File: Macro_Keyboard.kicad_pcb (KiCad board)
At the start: 6 copper layers, 109.7 x 84.3 mm, 103 parts, among them J1 USB_C_Receptacle_USB2.0, J2 USB_A, J3 USB_A, J4 USB_A, SW1 SW_Push, SW10 SW_DIP_x01, SW2 SW_DIP_x01, SW3 SW_DIP_x01, SW4 SW_DIP_x01, SW5 SW_DIP_x01, SW6 SW_DIP_x01, SW7 SW_DIP_x01, SW8 SW_DIP_x01, SW9 SW_DIP_x01, U1 STM32L432KCUx, U2 LD39050PU33R, U5 SRV05-4, U6 SRV05-4, Y1 12MHz

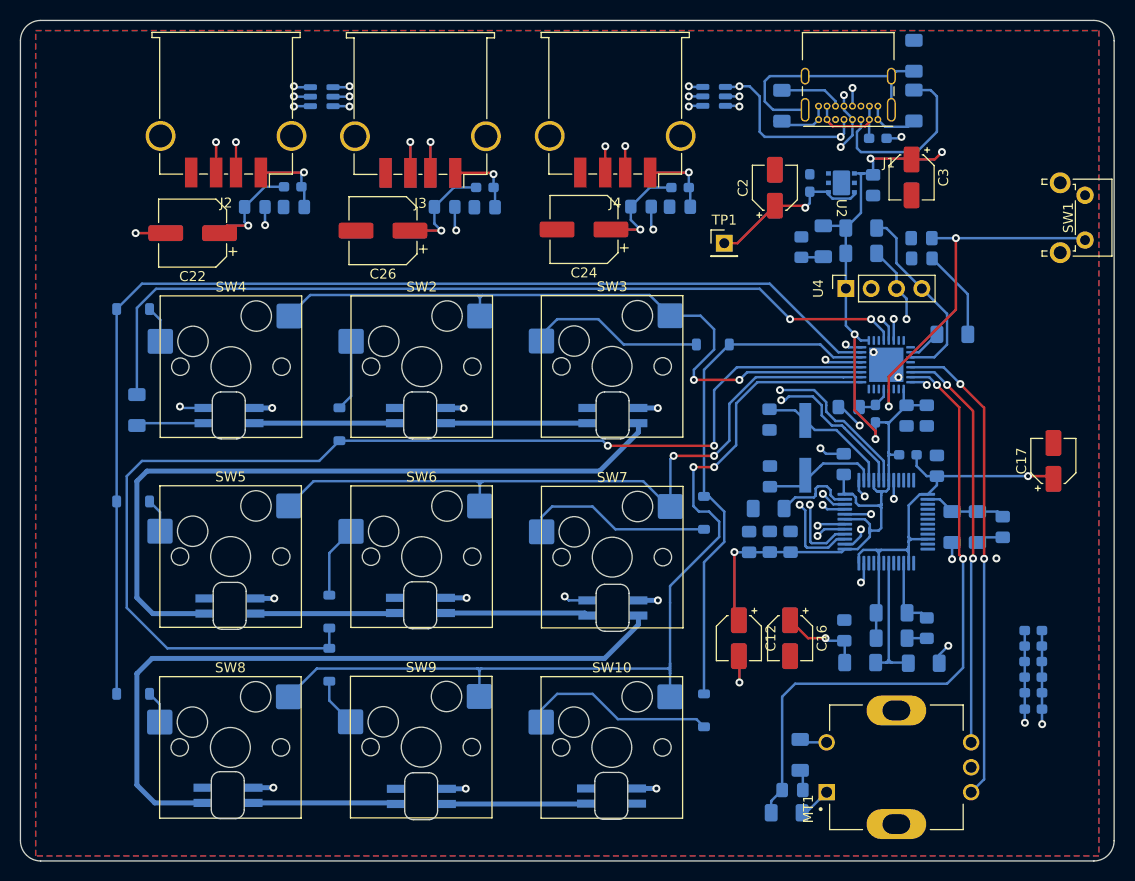
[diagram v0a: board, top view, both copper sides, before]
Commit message: Neue Anordnung für bessere Usb Leitungen
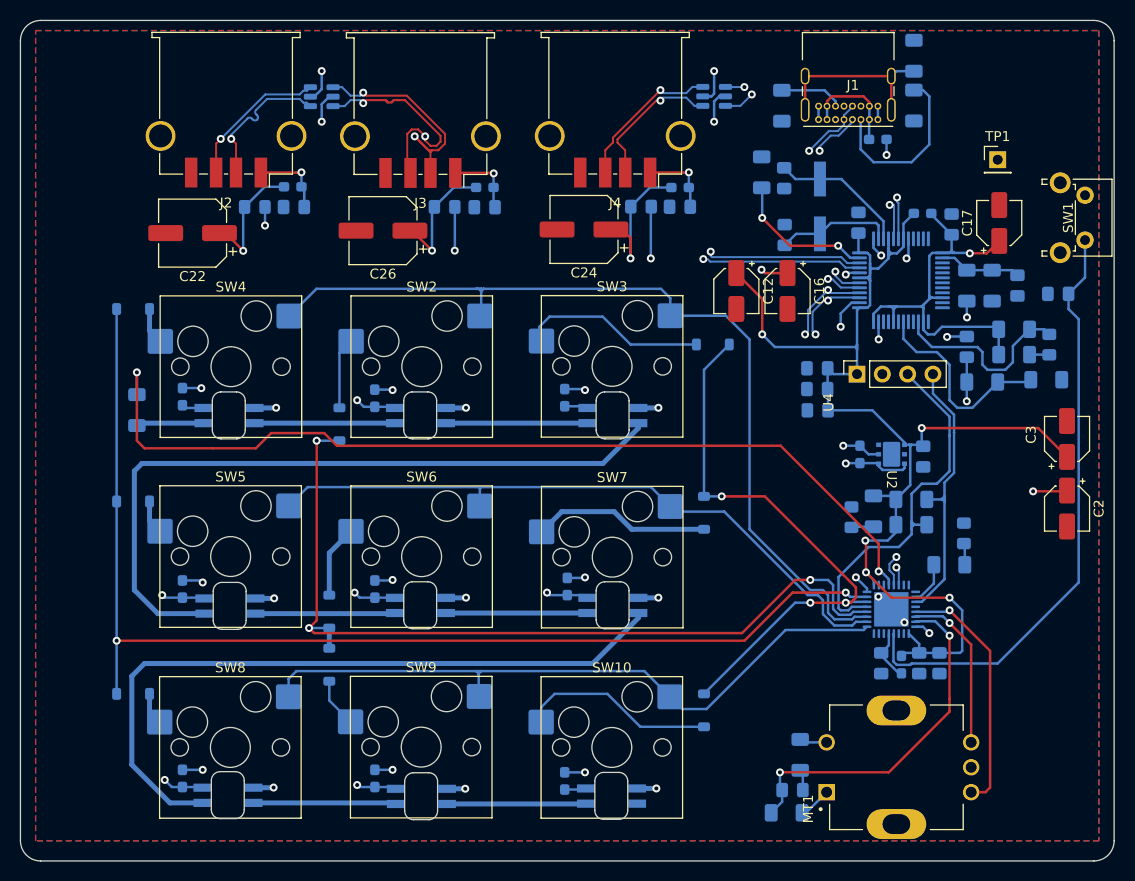
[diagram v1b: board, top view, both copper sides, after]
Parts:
- added C34: tbd, Capacitor_SMD:C_0603_1608Metric_Pad1.08x0.95mm_HandSolder, B.Cu at (73.2, 115.7)
- added C35: tbd, Capacitor_SMD:C_0603_1608Metric_Pad1.08x0.95mm_HandSolder, B.Cu at (92.5, 115.7)
- added C36: tbd, Capacitor_SMD:C_0603_1608Metric_Pad1.08x0.95mm_HandSolder, B.Cu at (111.5, 115.9)
- moved C33 88.5 mm to (73.2, 77.4), turned to -90 degrees
- moved C30 85.8 mm to (73.2, 96.7), turned to -90 degrees
- moved C32 70.6 mm to (92.4, 77.5), turned to -90 degrees
- moved C28 66.9 mm to (92.5, 96.7), turned to -90 degrees
- moved C31 53.9 mm to (111.5, 77.5), turned to -90 degrees
- moved C25 48.4 mm to (111.8, 96.4), turned to -90 degrees
- moved C2 43.5 mm to (161.9, 88.6), turned to -90 degrees
- moved C12 34.8 mm to (128.7, 66.8)
- moved C16 34.8 mm to (133.9, 66.8)
- moved R5 33.7 mm to (131.3, 54.9), turned to -90 degrees
- moved D3 31.0 mm to (160.1, 72.1)
- moved R8 31.0 mm to (156.6, 70.6)
- moved C15 31.0 mm to (151.8, 72.4)
- moved R11 31.0 mm to (159.8, 75.7)
- moved R9 31.0 mm to (156.6, 73.2)
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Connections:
- net /USB/DM1 renamed /USB/D_N1
- net /USB/DM2 renamed /USB/D_N2
- net /USB/DM3 renamed /USB/D_N3
- net /USB/DP1 renamed /USB/D_P1
- net /USB/DP2 renamed /USB/D_P2
- net /USB/DP3 renamed /USB/D_P3
- net USBDM renamed USBD_N
- net USBDP renamed USBD_P
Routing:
- net COL 1: track 119.2 -> 86.9 mm, vias 2 -> 3
- net Net-(U1-PH3): track 63.9 -> 35.8 mm
- net +3.3V: track 102.8 -> 128.6 mm
- net ROW 2: track 93.4 -> 68.5 mm, vias 2 -> 0
- net Rotary_B: track 41.2 -> 16.6 mm, vias 2 -> 1
- net Net-(U1-NRST): track 36.9 -> 60.4 mm, vias 2 -> 0
- net Rotary_A: track 48.2 -> 25.0 mm, vias 2 -> 1
- net ROW 0: track 70.6 -> 89.9 mm, vias 2 -> 0
- net SCK: track 22.9 -> 38.1 mm, vias 2 -> 0
- net /USB/D_P3: track 62.5 -> 47.6 mm, vias 3 -> 2
- net /USB/D_N3: track 59.7 -> 46.7 mm, vias 3 -> 2
- net /USB/PGANG: track 7.31 -> 19.4 mm
- net +5V: track 66.8 -> 76.0 mm, vias 20 -> 30
- net SDA: track 19.4 -> 28.2 mm
- net USBD_N: track 89.8 -> 81.6 mm
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
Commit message: Add files via upload
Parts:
- C10, C11, C13, C14, C15, C18, C19, C20, C21, C23, C27, C29, C9, D3, FB2, FB3, FB4, FB5, FB6, R10, R11, R12, R13, R17, R2, R3, R5, R6, R7, R8, R9, TH1, TH2, TH4, U3, U5, U6, Y1: moved to F.Cu
- C2, C3: moved to B.Cu
- moved C3 91.4 mm to (72.9, 60.6)
- moved C2 77.6 mm to (89.2, 61.2)
- moved C4 73.3 mm to (77.4, 61.8), turned to 90 degrees
- moved TP1 72.0 mm to (128.0, 120.3)
- moved U2 67.1 mm to (80.6, 62.1), turned to -90 degrees
- moved C1 61.1 mm to (83.7, 62.1), turned to -90 degrees
- moved TH1 44.2 mm to (124.5, 61.2)
- moved TH4 40.8 mm to (78.7, 63.8), turned to -90 degrees
- moved J2 39.4 mm to (116.9, 48.5)
- moved C22 39.4 mm to (113.6, 61.0)
- moved C23 39.4 mm to (123.7, 56.6), turned to 0 degrees
- moved C24 39.4 mm to (74.1, 60.6)
- moved J4 39.4 mm to (77.2, 48.5)
- moved U6 39.3 mm to (87.2, 47.0)
- moved C29 39.0 mm to (84.1, 56.9), turned to 0 degrees
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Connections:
- U5 pad 1: /USB/D_N2 -> /USB/D_P2
- U5 pad 3: /USB/D_P2 -> /USB/D_N2
- U5 pad 4: /USB/D_N1 -> /USB/D_P1
- U5 pad 6: /USB/D_P1 -> /USB/D_N1
- U6 pad 1: USBD_N -> USBD_P
- U6 pad 3: USBD_P -> USBD_N
- U6 pad 4: /USB/D_N3 -> /USB/D_P3
- U6 pad 6: /USB/D_P3 -> /USB/D_N3
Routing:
- net /USB/D_P1: track 96.7 -> 34.2 mm, vias 2 -> 0
- net /USB/D_N1: track 96.6 -> 34.2 mm, vias 2 -> 0
- net Net-(U1-NRST): track 60.4 -> 3.04 mm
- net GND: track 62.0 -> 9.63 mm, vias 18 -> 3
- net +3.3V: track 128.6 -> 84.1 mm, vias 5 -> 0
- net /USB/D_N3: track 46.7 -> 86.0 mm, vias 2 -> 0
- net /USB/D_P3: track 47.6 -> 86.2 mm, vias 2 -> 0
- net Net-(U1-PH3): track 35.8 -> 0.00 mm, vias 2 -> 0
- net ROW 0: track 89.9 -> 57.7 mm, vias 0 -> 2
- net Rotary_A: track 25.0 -> 0.00 mm, vias 1 -> 0
- net /USB/D_N2: track 77.7 -> 56.9 mm, vias 3 -> 0
- net /USB/D_P2: track 77.1 -> 57.0 mm, vias 3 -> 0
- net /USB/X1: track 11.8 -> 30.6 mm, vias 0 -> 2
- net ROW 2: track 68.5 -> 85.7 mm, vias 0 -> 2
- net Rotary_B: track 16.6 -> 0.00 mm, vias 1 -> 0
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- removed copper zone on In4.Cu, net GND
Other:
- board size 109.7 x 84.3 mm -> 95.6 x 84.2 mm
- copper layers 6 -> 4

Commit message: Add files via upload
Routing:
- net +3.3V: track 84.1 -> 174.9 mm, vias 0 -> 4
- net Net-(U1-NRST): track 3.04 -> 74.5 mm, vias 0 -> 2
- net GND: track 9.63 -> 75.5 mm, vias 3 -> 20
- net Net-(U1-PH3): track 0.00 -> 65.5 mm, vias 0 -> 1
- net Rotary_A: track 0.00 -> 62.0 mm, vias 0 -> 1
- net Rotary_B: track 0.00 -> 54.7 mm, vias 0 -> 1
- net Net-(J2-VBUS): track 0.00 -> 19.8 mm, vias 0 -> 2
- net Net-(U3-RREF): track 0.00 -> 14.2 mm, vias 0 -> 2
- net Net-(C22-Pad1): track 0.00 -> 8.57 mm
- net BOOT: track 0.00 -> 7.74 mm
- net +5V: track 70.1 -> 75.9 mm, vias 24 -> 27
- net Net-(FB6-Pad1): track 4.91 -> 10.3 mm
- net Net-(MT1-Pad2): track 0.00 -> 4.10 mm
- net USBD_N: track 86.6 -> 88.9 mm
- net USBD_P: track 86.6 -> 88.9 mm
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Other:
- board text added: "TODO if Route is okay: .) Name .) Silkscreen .) DRC"

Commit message: Add files via upload
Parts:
- removed C10, C11, C13, C18: 0.1uF, Capacitor_SMD:C_0805_2012Metric_Pad1.18x1.45mm_HandSolder
- removed C12: 1uF, Capacitor_SMD:CP_Elec_4x5.4
- removed C17: 10uF, Capacitor_SMD:CP_Elec_4x5.8
- removed FB5: BLM18BA, Inductor_SMD:L_0603_1608Metric_Pad1.05x0.95mm_HandSolder
- added C37: 1uF, Capacitor_SMD:C_0603_1608Metric_Pad1.08x0.95mm_HandSolder, F.Cu at (134.5, 54.4)
- added C38: 1uF, Capacitor_SMD:C_0603_1608Metric_Pad1.08x0.95mm_HandSolder, F.Cu at (134.6, 56.1)
- added C39: 1uF, Capacitor_SMD:C_0603_1608Metric_Pad1.08x0.95mm_HandSolder, F.Cu at (130.8, 56.1)
- added C40: 1uF, Capacitor_SMD:C_0603_1608Metric_Pad1.08x0.95mm_HandSolder, F.Cu at (134.5, 50.9)
- added C41: 0.1uF, Capacitor_SMD:C_0603_1608Metric_Pad1.08x0.95mm_HandSolder, F.Cu at (134.5, 49.2)
- added C42: 0.1uF, Capacitor_SMD:C_0603_1608Metric_Pad1.08x0.95mm_HandSolder, F.Cu at (130.8, 52.6)
- added FB7: BLM18BA, Inductor_SMD:L_0603_1608Metric_Pad1.05x0.95mm_HandSolder, F.Cu at (134.5, 52.6)
- added FB8: BLM18BA, Inductor_SMD:L_0603_1608Metric_Pad1.05x0.95mm_HandSolder, F.Cu at (130.8, 54.4)
- C14: value 0.1uF -> 10uF; footprint Capacitor_SMD:C_0805_2012Metric_Pad1.18x1.45mm_HandSolder -> Capacitor_SMD:CP_Elec_4x5.8; moved to B.Cu
- C15, C19, C23, C27, C29, C4, C5, C6, C7, C8, C9: footprint Capacitor_SMD:C_0805_2012Metric_Pad1.18x1.45mm_HandSolder -> Capacitor_SMD:C_0603_1608Metric_Pad1.08x0.95mm_HandSolder
- C16, C2, C3: footprint Capacitor_SMD:CP_Elec_4x5.4 -> Capacitor_SMD:C_0603_1608Metric_Pad1.08x0.95mm_HandSolder
- C20, C21: footprint Capacitor_SMD:C_0805_2012Metric_Pad1.18x1.45mm_HandSolder -> Capacitor_SMD:C_0603_1608Metric_Pad1.08x0.95mm_HandSolder; moved to B.Cu
- R1, R10, R11, R12, R13, R15, R16, R17, R2, R3, R4, R5, R6, R7, R8, R9: footprint Resistor_SMD:R_1206_3216Metric_Pad1.30x1.75mm_HandSolder -> Resistor_SMD:R_0805_2012Metric_Pad1.20x1.40mm_HandSolder
- Y1: moved to B.Cu
- moved C3 80.9 mm to (151.0, 81.8), turned to 180 degrees
- moved C4 75.9 mm to (151.1, 79.7), turned to 180 degrees
- moved U2 72.0 mm to (151.1, 76.2), turned to 0 degrees
- moved C1 68.4 mm to (151.3, 72.9), turned to 0 degrees
- moved C2 62.8 mm to (151.3, 70.9), turned to 0 degrees
- moved U4 29.7 mm to (145.8, 104.4), turned to -90 degrees
- moved C14 23.4 mm to (151.6, 85.3), turned to 180 degrees
- moved C21 22.0 mm to (142.0, 71.9), turned to 0 degrees
- moved C20 20.5 mm to (135.7, 72.0), turned to 180 degrees
- moved Y1 19.2 mm to (138.9, 68.6), turned to 0 degrees
- moved C16 19.2 mm to (138.5, 53.6), turned to 90 degrees
- moved R4 15.4 mm to (144.8, 78.0), turned to 0 degrees
- moved C6 15.0 mm to (137.4, 90.8), turned to 180 degrees
- moved C7 13.8 mm to (137.4, 89.0), turned to 180 degrees
- moved D2 13.2 mm to (144.8, 75.8), turned to 0 degrees
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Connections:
- C14 pad 1: DVDD -> +3.3V
- U3 pad 1: +3.3V -> AVDD
- U3 pad 12: +3.3V -> AVDD
- U3 pad 16: +3.3V -> AVDD
- U3 pad 19: +3.3V -> AVDD
- U3 pad 7: +3.3V -> AVDD
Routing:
- net +3.3V: track 174.9 -> 0.00 mm, vias 4 -> 0
- net COL 0: track 106.9 -> 0.00 mm
- net USBD_N: track 88.9 -> 0.00 mm, vias 1 -> 0
- net USBD_P: track 88.9 -> 0.00 mm, vias 1 -> 0
- net /USB/D_P3: track 86.2 -> 0.00 mm
- net /USB/D_N3: track 86.0 -> 0.00 mm
- net ROW 2: track 85.7 -> 0.00 mm, vias 2 -> 0
- net COL 1: track 81.9 -> 0.00 mm, vias 3 -> 0
- net LED: track 80.2 -> 0.00 mm, vias 2 -> 0
- net +5V: track 75.9 -> 0.00 mm, vias 27 -> 0
- net GND: track 75.5 -> 0.00 mm, vias 20 -> 0
- net Net-(U1-NRST): track 74.5 -> 0.00 mm, vias 2 -> 0
- net Net-(SK6812MINI_E3-DOUT): track 73.0 -> 0.00 mm
- net Net-(SK6812MINI_E6-DOUT): track 71.7 -> 0.00 mm
- net ROW 1: track 68.3 -> 0.00 mm, vias 2 -> 0
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- removed copper zone on In2.Cu, net +5V
- removed copper zone on B.Cu, net GND
- removed copper zone on F.Cu, net GND
- removed copper zone on In1.Cu, net GND
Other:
- board text removed: "TODO if Route is okay: .) Name .) Silkscreen .) DRC"

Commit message: Add files via upload
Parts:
- added C10: 0.1uF, Capacitor_SMD:C_0603_1608Metric_Pad1.08x0.95mm_HandSolder, B.Cu at (135.7, 49.3)
- added C11: 0.1uF, Capacitor_SMD:C_0603_1608Metric_Pad1.08x0.95mm_HandSolder, B.Cu at (135.7, 51.0)
- added C12: 0.1uF, Capacitor_SMD:C_0603_1608Metric_Pad1.08x0.95mm_HandSolder, B.Cu at (135.7, 52.7)
- added C13: 0.1uF, Capacitor_SMD:C_0603_1608Metric_Pad1.08x0.95mm_HandSolder, B.Cu at (135.7, 54.5)
- added C17: 0.1uF, Capacitor_SMD:C_0603_1608Metric_Pad1.08x0.95mm_HandSolder, F.Cu at (135.7, 49.3)
- added C18: 0.1uF, Capacitor_SMD:C_0603_1608Metric_Pad1.08x0.95mm_HandSolder, F.Cu at (135.7, 51.0)
- added C43: 0.1uF, Capacitor_SMD:C_0603_1608Metric_Pad1.08x0.95mm_HandSolder, F.Cu at (135.7, 52.7)
- added C44: 0.1uF, Capacitor_SMD:C_0603_1608Metric_Pad1.08x0.95mm_HandSolder, F.Cu at (135.7, 54.5)
- C22, C23, C38, C39, C42, FB3, FB8, TH1: moved to B.Cu
- moved C29 18.5 mm to (66.5, 54.5), turned to 90 degrees
- moved FB4 14.7 mm to (66.4, 57.9), turned to -90 degrees
- moved TH4 13.0 mm to (68.3, 57.7), turned to 90 degrees
- moved C23 12.4 mm to (112.4, 61.3), turned to 180 degrees
- moved TH1 9.19 mm to (112.3, 57.9)
- moved FB3 8.83 mm to (112.4, 59.7)
- moved C22 8.49 mm to (105.7, 57.9)
- moved FB2 7.84 mm to (93.1, 61.2)
- moved C27 7.80 mm to (96.5, 61.2)
- moved TH2 5.95 mm to (94.5, 59.2)
- moved C26 5.84 mm to (87.6, 59.2)
- moved C39 3.72 mm to (132.3, 52.7)
- moved FB8 3.67 mm to (132.3, 51.0), turned to 0 degrees
- moved C42 3.59 mm to (132.2, 49.3), turned to 0 degrees
- moved C38 2.79 mm to (132.3, 54.5)
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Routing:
- net +3.3V: track 0.00 -> 119.0 mm, vias 0 -> 4
- net COL 0: track 0.00 -> 109.7 mm, vias 0 -> 2
- net +5V: track 0.00 -> 97.1 mm, vias 0 -> 25
- net USBD_P: track 0.00 -> 92.7 mm, vias 0 -> 1
- net USBD_N: track 0.00 -> 92.0 mm, vias 0 -> 1
- net LED: track 0.00 -> 89.2 mm, vias 0 -> 2
- net /USB/D_N3: track 0.00 -> 88.4 mm
- net /USB/D_P3: track 0.00 -> 87.2 mm
- net ROW 2: track 0.00 -> 81.8 mm, vias 0 -> 2
- net GND: track 0.00 -> 78.8 mm, vias 0 -> 26
- net Net-(SK6812MINI_E3-DOUT): track 0.00 -> 73.7 mm
- net Net-(SK6812MINI_E6-DOUT): track 0.00 -> 71.6 mm
- net COL 1: track 0.00 -> 70.7 mm, vias 0 -> 2
- net ROW 0: track 0.00 -> 70.2 mm, vias 0 -> 4
- net ROW 1: track 0.00 -> 67.3 mm, vias 0 -> 2
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- added copper zone on In2.Cu, net +5V
- added copper zone on B.Cu, net AVDD
- added copper zone on In2.Cu, net DVDD
- added copper zone on B.Cu, net GND
- added copper zone on F.Cu, net GND
- added copper zone on In1.Cu, net GND

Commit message: Add files via upload
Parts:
- C22, C23, FB3, TH1: moved to F.Cu
- moved SK6812MINI_E7 42.2 mm to (118.1, 118.8), turned to 180 degrees
- moved SK6812MINI_E1 42.1 mm to (118.2, 80.7), turned to 180 degrees
- moved SK6812MINI_E4 42.0 mm to (118.1, 99.8), turned to 180 degrees
- moved SK6812MINI_E3 35.1 mm to (79.7, 80.7), turned to 180 degrees
- moved SK6812MINI_E6 35.1 mm to (79.7, 99.8), turned to 180 degrees
- moved SK6812MINI_E9 35.0 mm to (79.7, 118.8), turned to 180 degrees
- moved U5 25.6 mm to (130.3, 57.4), turned to 180 degrees
- moved R15 13.7 mm to (137.4, 92.7), turned to 180 degrees
- moved D8 6.77 mm to (87.1, 105.7)
- moved D9 6.77 mm to (87.1, 111.0)
- moved R5 6.44 mm to (128.3, 68.6), turned to 90 degrees
- moved C28 6.06 mm to (87.4, 93.4)
- moved D3 4.80 mm to (153.9, 62.0)
- moved R8 4.80 mm to (152.9, 58.9)
- moved R9 4.80 mm to (155.0, 58.9)
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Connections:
- J1 pad A6: USBD_P -> /USB/D_P0
- J1 pad A7: USBD_N -> /USB/D_N0
- J1 pad B6: USBD_P -> /USB/D_P0
- J1 pad B7: USBD_N -> /USB/D_N0
- U1 pad 14: COL 2 -> COL 0
- U1 pad 15: COL 0 -> COL 2
- U3 pad 21: unconnected-(U3-DM4-Pad21) -> USBD_N
- U3 pad 22: unconnected-(U3-DP4-Pad22) -> USBD_P
- U3 pad 3: USBD_N -> /USB/D_N0
- U3 pad 4: USBD_P -> /USB/D_P0
- U5 pad 1: /USB/D_P2 -> /USB/D_P0
- U5 pad 3: /USB/D_N2 -> /USB/D_N0
- U5 pad 4: /USB/D_P1 -> /USB/D_N1
- U5 pad 6: /USB/D_N1 -> /USB/D_P1
- U6 pad 1: USBD_P -> /USB/D_P2
- U6 pad 3: USBD_N -> /USB/D_N2
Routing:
- net +3.3V: track 119.0 -> 0.00 mm, vias 4 -> 0
- net COL 0: track 109.7 -> 0.00 mm, vias 2 -> 0
- net +5V: track 97.1 -> 0.00 mm, vias 25 -> 0
- net LED: track 89.2 -> 0.00 mm, vias 2 -> 0
- net ROW 2: track 81.8 -> 0.00 mm, vias 2 -> 0
- net GND: track 78.8 -> 0.00 mm, vias 26 -> 0
- net USBD_P: track 92.7 -> 15.6 mm
- net USBD_N: track 92.0 -> 15.6 mm
- net Net-(SK6812MINI_E3-DOUT): track 73.7 -> 0.00 mm
- net Net-(SK6812MINI_E6-DOUT): track 71.6 -> 0.00 mm
- net COL 1: track 70.7 -> 0.00 mm, vias 2 -> 0
- net ROW 0: track 70.2 -> 0.00 mm, vias 4 -> 0
- net ROW 1: track 67.3 -> 0.00 mm, vias 2 -> 0
- net COL 2: track 54.4 -> 0.00 mm, vias 2 -> 0
- net Net-(U1-NRST): track 48.2 -> 0.00 mm, vias 2 -> 0
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- removed copper zone on In2.Cu, net +5V
- removed copper zone on B.Cu, net AVDD
- removed copper zone on In2.Cu, net DVDD
- removed copper zone on B.Cu, net GND
- removed copper zone on F.Cu, net GND
- removed copper zone on In1.Cu, net GND
